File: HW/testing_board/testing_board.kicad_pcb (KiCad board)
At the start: 2 copper layers, 65 x 56 mm, 70 parts, among them J1 GPIO, J2 Left_, J3 Right_, J4 SWD, J5 OLED, SW1 Start, U1 TPS22917DBV, U2 CD4051BM96, U3 CD4051BM96, U4 CD4051BM96

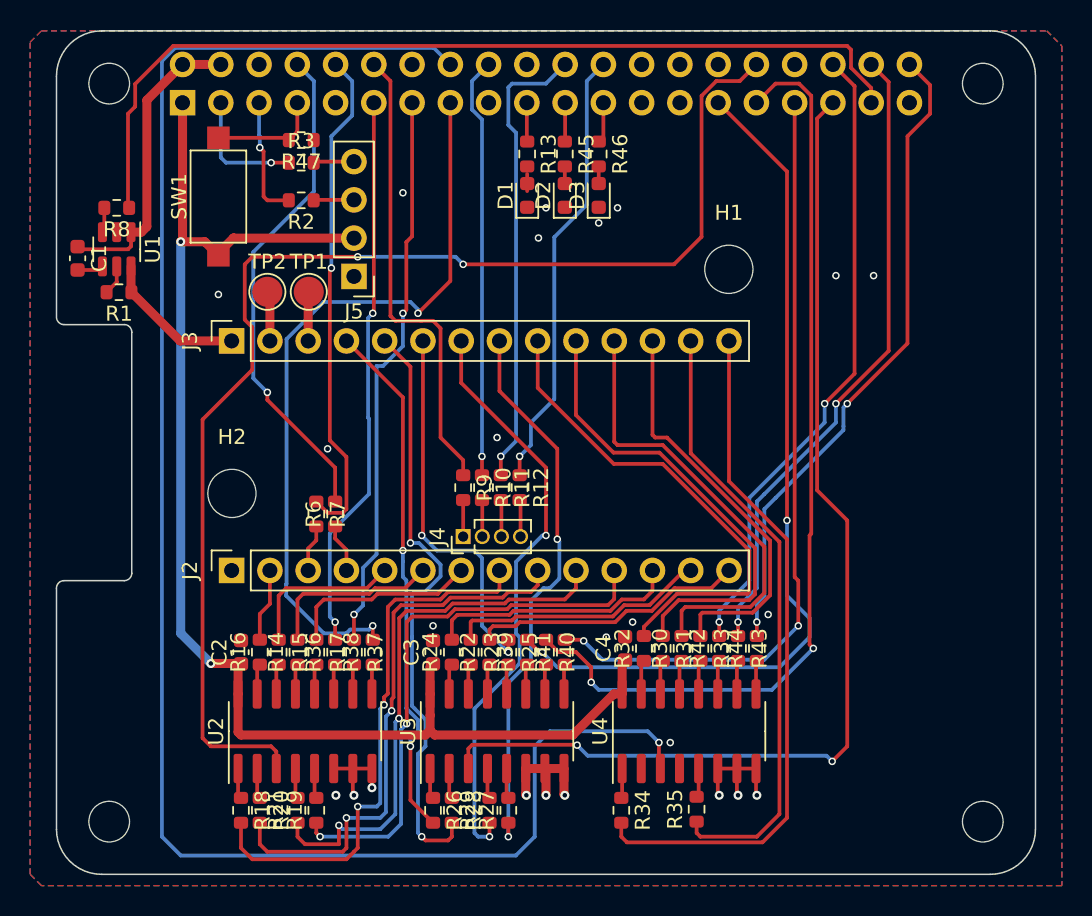
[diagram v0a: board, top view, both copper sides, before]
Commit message: add sd card file library+ new HW version
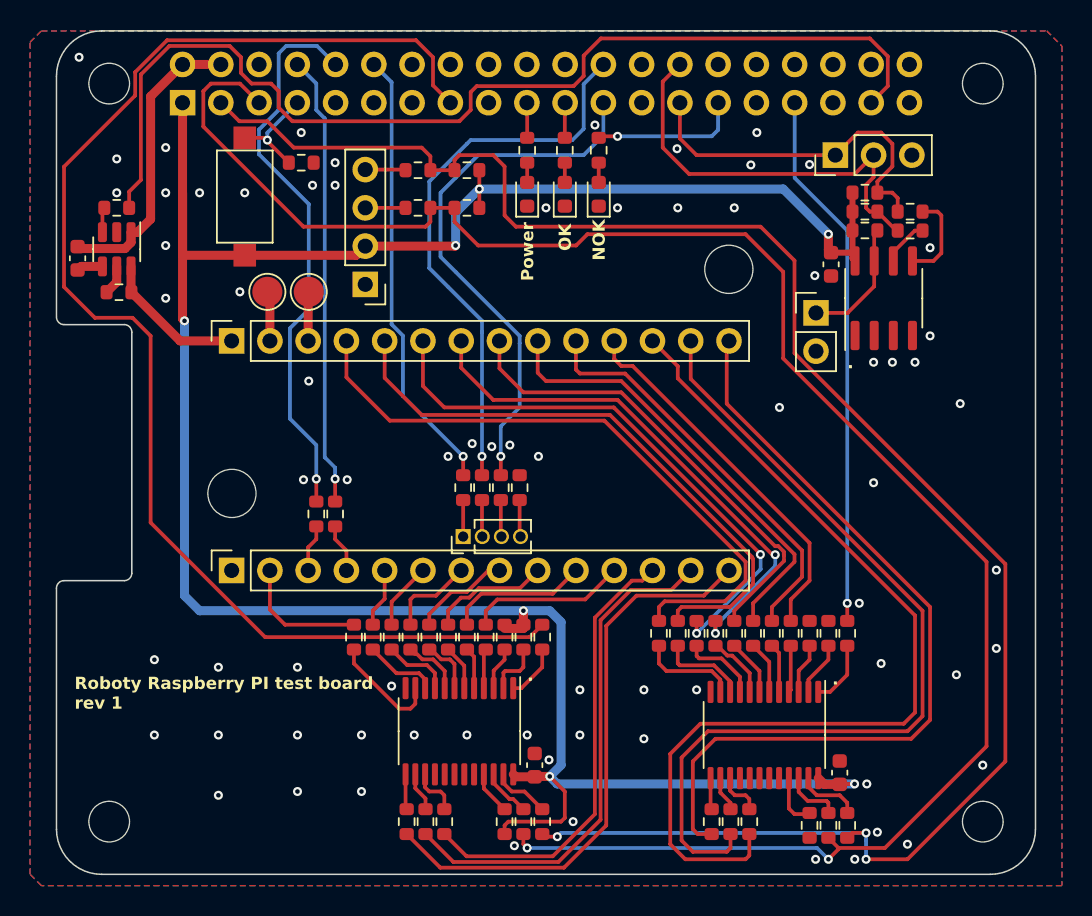
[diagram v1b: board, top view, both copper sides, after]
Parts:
- removed U4: CD4051BM96, Package_SO:SOIC-16_3.9x9.9mm_P1.27mm
- added J6: WP_jumper, Connector_PinHeader_2.54mm:PinHeader_1x02_P2.54mm_Vertical, F.Cu at (150.4, 62.7)
- added J7: I2C_prob, Connector_PinHeader_2.54mm:PinHeader_1x03_P2.54mm_Vertical, F.Cu at (151.7, 52.2)
- added R4: 1k, Resistor_SMD:R_0603_1608Metric, F.Cu at (129.8, 96.5)
- added R48: 1k, Resistor_SMD:R_0603_1608Metric, F.Cu at (150.0, 96.8)
- added R49: 10k, Resistor_SMD:R_0603_1608Metric, F.Cu at (127.2, 53.2)
- added R5: 1k, Resistor_SMD:R_0603_1608Metric, F.Cu at (131.0, 84.2)
- added R50: 10k, Resistor_SMD:R_0603_1608Metric, F.Cu at (127.2, 55.8)
- added R51: 10k, Resistor_SMD:R_0603_1608Metric, F.Cu at (153.7, 57.2)
- added R52: 10k, Resistor_SMD:R_0603_1608Metric, F.Cu at (153.7, 54.7)
- added R53: 10k, Resistor_SMD:R_0603_1608Metric, F.Cu at (153.7, 56.0)
- added R54: 0, Resistor_SMD:R_0603_1608Metric, F.Cu at (156.7, 56.0)
- added R55: 0, Resistor_SMD:R_0603_1608Metric, F.Cu at (156.7, 57.3)
- added U5: TCA9555PWR, Package_SO:TSSOP-24_4.4x7.8mm_P0.65mm, F.Cu at (126.8, 90.5)
- R13, R45, R46: value 560 -> 1k
- R42, R43, R44: value 0 -> 1k
- U2: value CD4051BM96 -> TCA9555PWR; footprint Package_SO:SOIC-16_3.9x9.9mm_P1.27mm -> Package_SO:TSSOP-24_4.4x7.8mm_P0.65mm
- U3: value CD4051BM96 -> CAT24C32; footprint Package_SO:SOIC-16_3.9x9.9mm_P1.27mm -> Package_SO:SOIC-8_3.9x4.9mm_P1.27mm
- moved U3 38.5 mm to (154.9, 61.8)
- moved U2 30.5 mm to (147.0, 90.8), turned to -90 degrees
- moved C4 28.9 mm to (151.4, 59.5), turned to -90 degrees
- moved C3 28.2 mm to (152.0, 93.2)
- moved R26 25.4 mm to (147.5, 84.0), turned to 90 degrees
- moved R39 24.2 mm to (152.5, 96.8), turned to -90 degrees
- moved R40 22.0 mm to (151.2, 96.8), turned to 90 degrees
- moved C2 20.9 mm to (131.8, 92.8)
- moved R25 18.8 mm to (148.8, 84.0)
- moved R41 18.8 mm to (152.5, 84.0)
- moved R36 17.8 mm to (132.2, 96.5), turned to -90 degrees
- moved R22 17.5 mm to (146.2, 84.0)
- moved R23 17.5 mm to (145.0, 84.0)
- moved R24 17.5 mm to (143.8, 84.0)
- moved R18 16.1 mm to (123.5, 84.2), turned to 90 degrees
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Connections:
- R10 pad 1: /GPIO24 -> /GPIO8/SPI0.CE0
- R11 pad 1: /GPIO25 -> /GPIO11/SPI0.SCLK
- R12 pad 1: /GPIO8/SPI0.CE0 -> unconnected-(R12-Pad1)
- R14 pad 1: Net-(U2-X0) -> Net-(U5-P00)
- R14 pad 2: HDR_LFT_PA2 -> HDR_RGT_PB5
- R15 pad 1: HDR_LFT_PA3 -> HDR_LFT_PB4
- R15 pad 2: Net-(U2-X1) -> Net-(U5-P01)
- R16 pad 1: Net-(U2-X2) -> Net-(U5-P02)
- R16 pad 2: HDR_LFT_PA8 -> HDR_LFT_PA15
- R17 pad 1: HDR_LFT_PA1 -> HDR_LFT_PA0
- R17 pad 2: Net-(U2-X3) -> Net-(U5-P03)
- R18 pad 1: Net-(U2-X4) -> Net-(U5-P04)
- R18 pad 2: HDR_LFT_PA0 -> HDR_LFT_PA1
- R19 pad 1: HDR_RGT_PB5 -> HDR_LFT_PA2
- R19 pad 2: Net-(U2-X5) -> Net-(U5-P05)
- R20 pad 1: Net-(U2-X6) -> Net-(U5-P06)
- R20 pad 2: HDR_LFT_PA15 -> HDR_LFT_PA3
- R21 pad 1: HDR_LFT_PB4 -> HDR_LFT_PA8
- R21 pad 2: Net-(U2-X7) -> Net-(U5-P07)
- R22 pad 1: Net-(U3-X0) -> Net-(U2-P02)
- R22 pad 2: HDR_RGT_PB9 -> HDR_LFT_PA6
- R23 pad 1: HDR_RGT_PB8 -> HDR_LFT_PA7
- R23 pad 2: Net-(U3-X1) -> Net-(U2-P03)
- R24 pad 1: Net-(U3-X2) -> Net-(U2-P04)
- R24 pad 2: HDR_RGT_PB7 -> HDR_RGT_PB10
- R25 pad 1: HDR_RGT_PB12 -> HDR_LFT_PA4
- R25 pad 2: Net-(U3-X3) -> Net-(U2-P00)
- R26 pad 1: Net-(U3-X4) -> Net-(U2-P01)
- R26 pad 2: HDR_RGT_PB14 -> HDR_LFT_PA5
- R27 pad 1: HDR_LFT_PA7 -> HDR_RGT_PB9
- R27 pad 2: Net-(U3-X5) -> Net-(U5-P10)
- R28 pad 1: Net-(U3-X6) -> Net-(U5-P11)
- R28 pad 2: HDR_RGT_PB13 -> HDR_RGT_PB8
- R29 pad 1: HDR_RGT_PB10 -> HDR_RGT_PB7
- R29 pad 2: Net-(U3-X7) -> Net-(U5-P12)
- R30 pad 1: Net-(U4-X0) -> Net-(U2-P05)
- R30 pad 2: HDR_LFT_PA4 -> HDR_RGT_PB12
- R31 pad 1: HDR_LFT_PA5 -> HDR_RGT_PB13
- R31 pad 2: Net-(U4-X1) -> Net-(U2-P06)
- R32 pad 1: Net-(U4-X2) -> Net-(U2-P07)
- R32 pad 2: HDR_LFT_PA6 -> HDR_RGT_PB14
- R33 pad 1: HDR_RGT_PB15 -> HDR_RGT_PC0
- R33 pad 2: Net-(U4-X3) -> Net-(U2-P10)
- R34 pad 1: Net-(U4-X4) -> Net-(U2-P11)
- R34 pad 2: HDR_RGT_PC0 -> HDR_RGT_PC1
- R35 pad 1: HDR_RGT_PC1 -> HDR_RGT_PB15
- R35 pad 2: Net-(U4-X5) -> Net-(U2-P12)
- R36 pad 1: /A1 -> Net-(U5-SDA)
- R36 pad 2: /GPIO17 -> /GPIO2/SDA1
- R37 pad 1: /GPIO27 -> /GPIO3/SCL1
- R37 pad 2: /B1 -> Net-(U5-SCL)
- R38 pad 1: /C1 -> Net-(U5-~{INT})
- R39 pad 2: /GPIO5 -> /GPIO2/SDA1
- R40 pad 1: /GPIO6 -> /GPIO3/SCL1
- R42 pad 1: /A3 -> +3V3
- R42 pad 2: /GPIO16 -> Net-(U5-A2)
- R43 pad 1: /GPIO20/PCM.DIN -> GND
- R43 pad 2: /B3 -> Net-(U2-A2)
- R44 pad 1: /C3 -> Net-(U2-A1)
- R44 pad 2: /GPIO21/PCM.DOUT -> GND
- R46 pad 1: /GPIO11/SPI0.SCLK -> /GPIO5
- U2 pad 1: Net-(U2-X4) -> /C2
- U2 pad 10: /B1 -> Net-(U2-P06)
- U2 pad 11: /A1 -> Net-(U2-P07)
- U2 pad 12: Net-(U2-X3) -> GND
- U2 pad 13: Net-(U2-X0) -> Net-(U2-P10)
- U2 pad 14: Net-(U2-X1) -> Net-(U2-P11)
- U2 pad 15: Net-(U2-X2) -> Net-(U2-P12)
- U2 pad 16: +3V3 -> unconnected-(U2-P13-Pad16)
- U2 pad 2: Net-(U2-X6) -> Net-(U2-A1)
- U2 pad 3: /OUT_MUX1 -> Net-(U2-A2)
- U2 pad 4: Net-(U2-X7) -> Net-(U2-P00)
- U2 pad 5: Net-(U2-X5) -> Net-(U2-P01)
- U2 pad 6: GND -> Net-(U2-P02)
- U2 pad 7: GND -> Net-(U2-P03)
- U2 pad 8: GND -> Net-(U2-P04)
- U2 pad 9: /C1 -> Net-(U2-P05)
- U3 pad 1: Net-(U3-X4) -> GND
- U3 pad 2: Net-(U3-X6) -> GND
- U3 pad 3: /OUT_MUX2 -> GND
- U3 pad 4: Net-(U3-X7) -> GND
- U3 pad 5: Net-(U3-X5) -> Net-(U3-SDA)
- U3 pad 6: GND -> Net-(U3-SCL)
- U3 pad 7: GND -> Net-(J6-Pin_1)
- U3 pad 8: GND -> +3V3
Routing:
- net /GPIO3/SCL1: track 8.13 -> 125.1 mm, vias 1 -> 2
- net /OUT_MUX3: track 114.0 -> 0.00 mm, vias 1 -> 0
- net /GPIO2/SDA1: track 8.30 -> 121.9 mm, vias 1 -> 3
- net /OUT_MUX1: track 84.8 -> 0.00 mm, vias 2 -> 0
- net +3V3: track 91.0 -> 166.8 mm, vias 2 -> 7
- net /OUT_MUX2: track 71.4 -> 0.00 mm, vias 2 -> 0
- net /GPIO6: track 62.2 -> 0.00 mm, vias 2 -> 0
- net /GPIO5: track 58.3 -> 9.95 mm, vias 2 -> 1
- net /GPIO21/PCM.DOUT: track 43.3 -> 0.00 mm, vias 2 -> 0
- net /GPIO20/PCM.DIN: track 42.6 -> 0.00 mm, vias 2 -> 0
- net /GPIO16: track 42.3 -> 0.00 mm, vias 2 -> 0
- net /GPIO22: track 50.0 -> 89.8 mm, vias 2 -> 0
- net /GPIO27: track 37.5 -> 0.00 mm, vias 2 -> 0
- net /GPIO17: track 37.1 -> 0.00 mm, vias 2 -> 0
- net HDR_RGT_PB15: track 27.2 -> 62.5 mm
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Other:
- board text added: "."
- board text added: "NOK"
- board text added: "OK"
- board text added: "Power"
- board text added: "Roboty Raspberry PI test board rev 1"
